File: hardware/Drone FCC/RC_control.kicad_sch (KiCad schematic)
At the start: 6 parts, among them J401 DSM Spektrum JST, J402 PPM Dupont

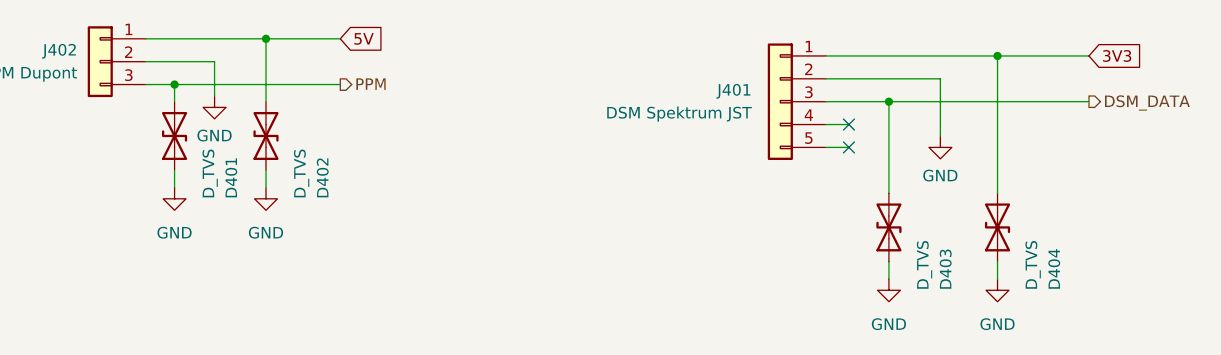
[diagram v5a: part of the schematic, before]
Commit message: removed all the TVS from the PCB and SCH
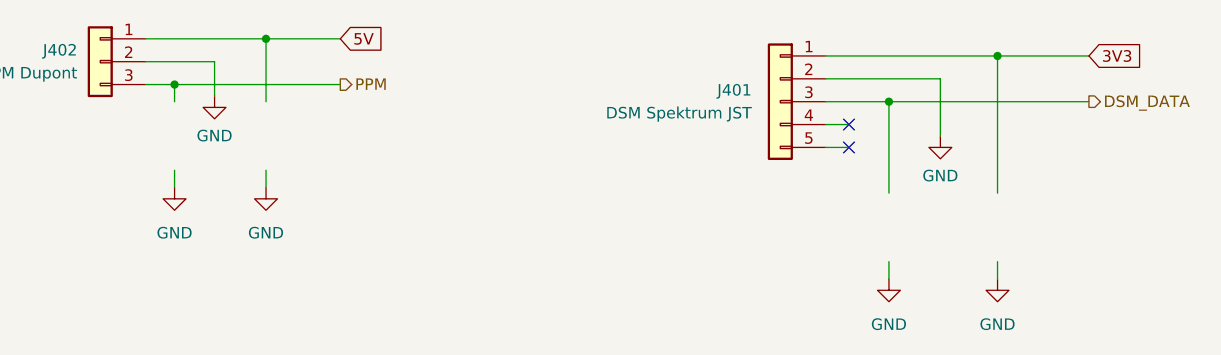
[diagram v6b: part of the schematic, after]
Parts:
- removed D401, D402, D403, D404: D_TVS, Diode_SMD:D_0402_1005Metric_Pad0.77x0.64mm_HandSolder, symbol Device:D_TVS
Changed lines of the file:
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@@
     (pin "1")
-  )
-  (symbol (lib_id "Device:D_TVS") (at 45.085 46.355 90) (unit 1)
-    (in_bom yes) (on_board yes)
-    (property "Reference" "D401" (id 0) (at 51.435 53.34 0)
-      (effects (font (size 1.27 1.27)) (justify left))
-    )
-    (property "Value" "D_TVS" (id 1) (at 48.895 53.34 0)
-      (effects (font (size 1.27 1.27)) (justify left))
-    )
-    (property "Footprint" "Diode_SMD:D_0402_1005Metric_Pad0.77x0.64mm_HandSolder" (id 2) (at 45.085 46.355 0)
-      (effects (font (size 1.27 1.27)) hide)
-    )
-    (property "Datasheet" "~" (id 3) (at 45.085 46.355 0)
-      (effects (font (size 1.27 1.27)) hide)
-    )
-    (pin "1")
-    (pin "2")
-  )
-  (symbol (lib_id "Device:D_TVS") (at 136.525 56.515 90) (unit 1)
-    (in_bom yes) (on_board yes)
-    (property "Reference" "D404" (id 0) (at 142.875 63.5 0)
-      (effects (font (size 1.27 1.27)) (justify left))
-    )
-    (property "Value" "D_TVS" (id 1) (at 140.335 63.5 0)
-      (effects (font (size 1.27 1.27)) (justify left))
-    )
-    (property "Footprint" "Diode_SMD:D_0402_1005Metric_Pad0.77x0.64mm_HandSolder" (id 2) (at 136.525 56.515 0)
-      (effects (font (size 1.27 1.27)) hide)
-    )
-    (property "Datasheet" "~" (id 3) (at 136.525 56.515 0)
-      (effects (font (size 1.27 1.27)) hide)
-    )
-    (pin "1")
-    (pin "2")
   )
   (symbol (lib_id "Connector_Generic:Conn_01x03") (at 36.83 38.1 0) (mirror y) (unit 1)
@@
     (pin "1")
   )
-  (symbol (lib_id "Device:D_TVS") (at 124.46 56.515 90) (unit 1)
-    (in_bom yes) (on_board yes)
-    (property "Reference" "D403" (id 0) (at 130.81 63.5 0)
-      (effects (font (size 1.27 1.27)) (justify left))
-    )
-    (property "Value" "D_TVS" (id 1) (at 128.27 63.5 0)
-      (effects (font (size 1.27 1.27)) (justify left))
-    )
-    (property "Footprint" "Diode_SMD:D_0402_1005Metric_Pad0.77x0.64mm_HandSolder" (id 2) (at 124.46 56.515 0)
-      (effects (font (size 1.27 1.27)) hide)
-    )
-    (property "Datasheet" "~" (id 3) (at 124.46 56.515 0)
-      (effects (font (size 1.27 1.27)) hide)
-    )
-    (pin "1")
-    (pin "2")
-  )
-  (symbol (lib_id "Device:D_TVS") (at 55.245 46.355 90) (unit 1)
-    (in_bom yes) (on_board yes)
-    (property "Reference" "D402" (id 0) (at 61.595 53.34 0)
-      (effects (font (size 1.27 1.27)) (justify left))
-    )
-    (property "Value" "D_TVS" (id 1) (at 59.055 53.34 0)
-      (effects (font (size 1.27 1.27)) (justify left))
-    )
-    (property "Footprint" "Diode_SMD:D_0402_1005Metric_Pad0.77x0.64mm_HandSolder" (id 2) (at 55.245 46.355 0)
-      (effects (font (size 1.27 1.27)) hide)
-    )
-    (property "Datasheet" "~" (id 3) (at 55.245 46.355 0)
-      (effects (font (size 1.27 1.27)) hide)
-    )
-    (pin "1")
-    (pin "2")
-  )
 )

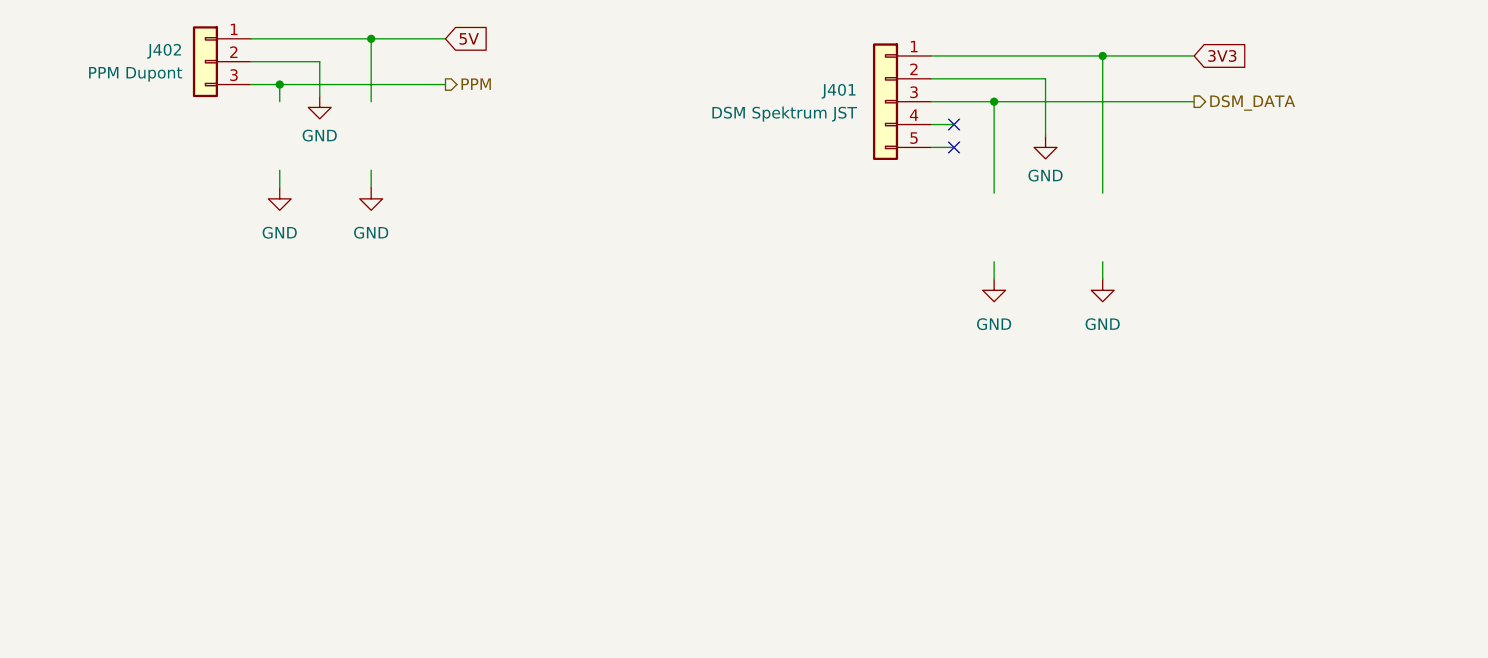
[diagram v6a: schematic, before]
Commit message: tidying up the schematic
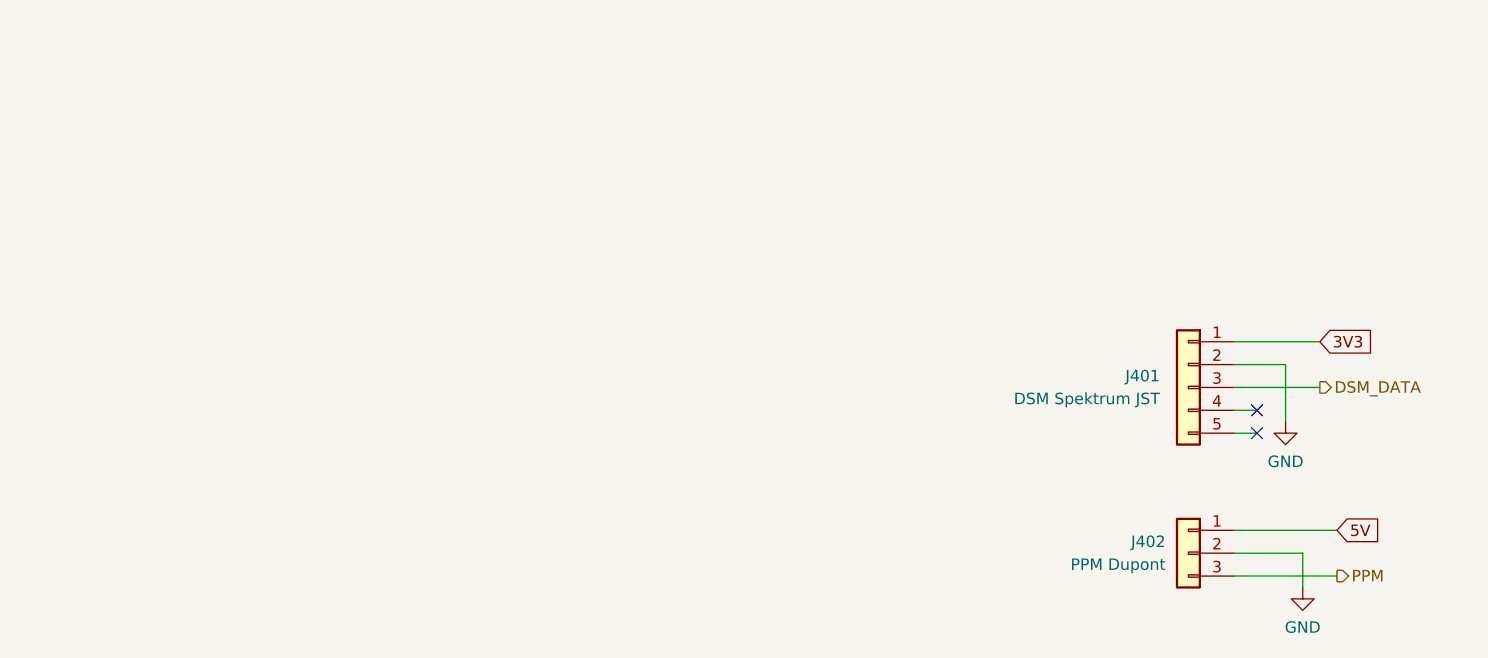
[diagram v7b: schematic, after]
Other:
- moved on the sheet: J401, J402

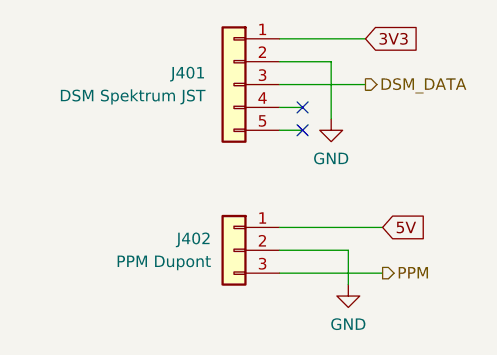
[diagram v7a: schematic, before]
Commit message: re enumeation of componentes
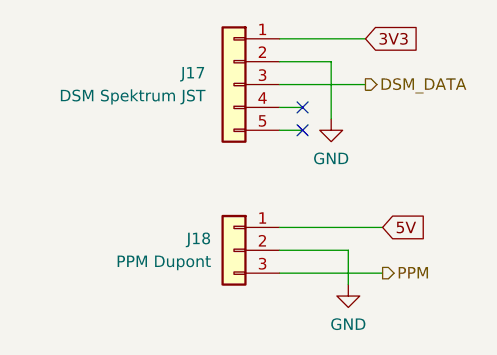
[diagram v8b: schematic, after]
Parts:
- renumbered J401 to J17, J402 to J18
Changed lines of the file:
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@@
   (symbol (lib_id "Connector_Generic:Conn_01x05") (at 146.05 74.295 0) (mirror y) (unit 1)
     (in_bom yes) (on_board yes) (fields_autoplaced)
-    (property "Reference" "J401" (id 0) (at 142.875 73.0249 0)
+    (property "Reference" "J17" (id 0) (at 142.875 73.0249 0)
       (effects (font (size 1.27 1.27)) (justify left))
     )
@@
   (symbol (lib_id "Connector_Generic:Conn_01x03") (at 146.05 92.71 0) (mirror y) (unit 1)
     (in_bom yes) (on_board yes) (fields_autoplaced)
-    (property "Reference" "J402" (id 0) (at 143.51 91.4399 0)
+    (property "Reference" "J18" (id 0) (at 143.51 91.4399 0)
       (effects (font (size 1.27 1.27)) (justify left))
     )
@@
   (symbol (lib_id "power:GND") (at 158.75 96.52 0) (mirror y) (unit 1)
     (in_bom yes) (on_board yes) (fields_autoplaced)
-    (property "Reference" "#PWR0120" (id 0) (at 158.75 102.87 0)
+    (property "Reference" "#PWR026" (id 0) (at 158.75 102.87 0)
       (effects (font (size 1.27 1.27)) hide)
     )
@@
   (symbol (lib_id "power:GND") (at 156.845 78.105 0) (mirror y) (unit 1)
     (in_bom yes) (on_board yes) (fields_autoplaced)
-    (property "Reference" "#PWR0119" (id 0) (at 156.845 84.455 0)
+    (property "Reference" "#PWR025" (id 0) (at 156.845 84.455 0)
       (effects (font (size 1.27 1.27)) hide)
     )
